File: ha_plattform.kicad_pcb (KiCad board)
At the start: 2 copper layers, 55 x 55 mm, 15 parts, among them J3 Raspberry_Pi_2_3

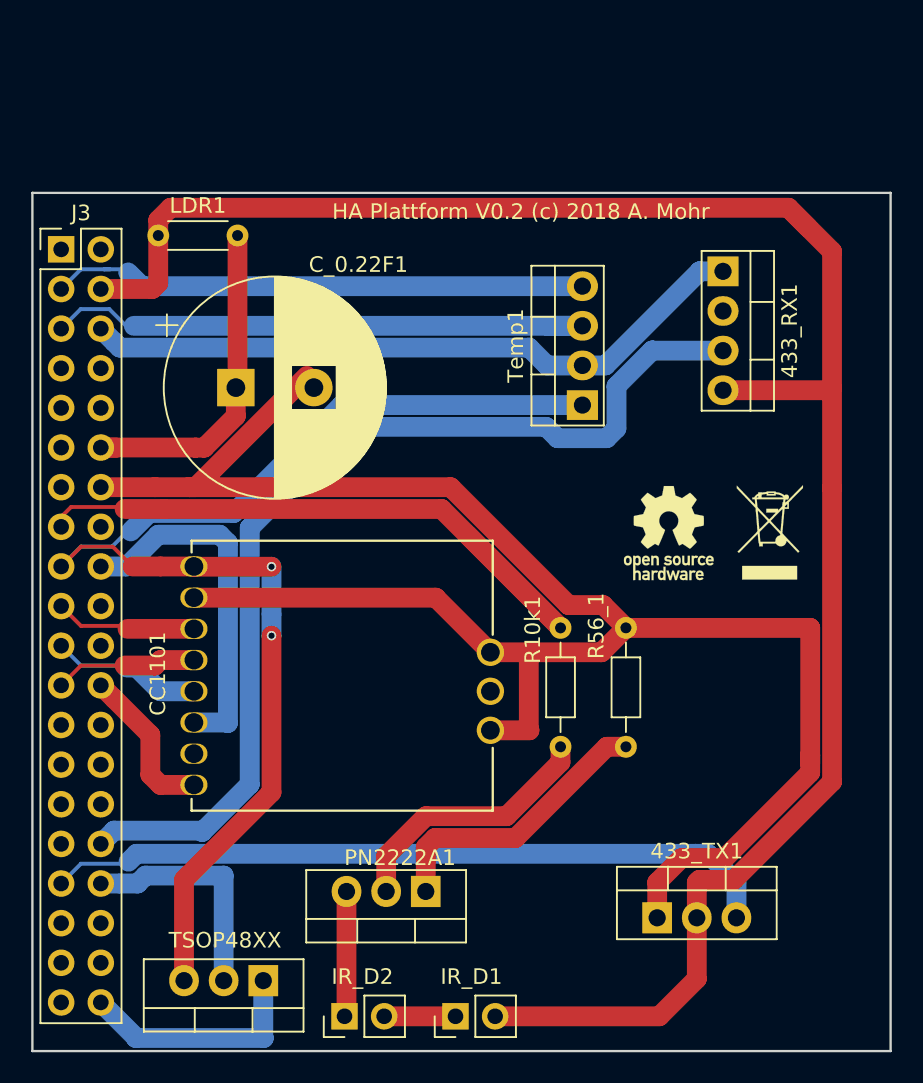
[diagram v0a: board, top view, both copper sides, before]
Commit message: reduced footprint for capacitor
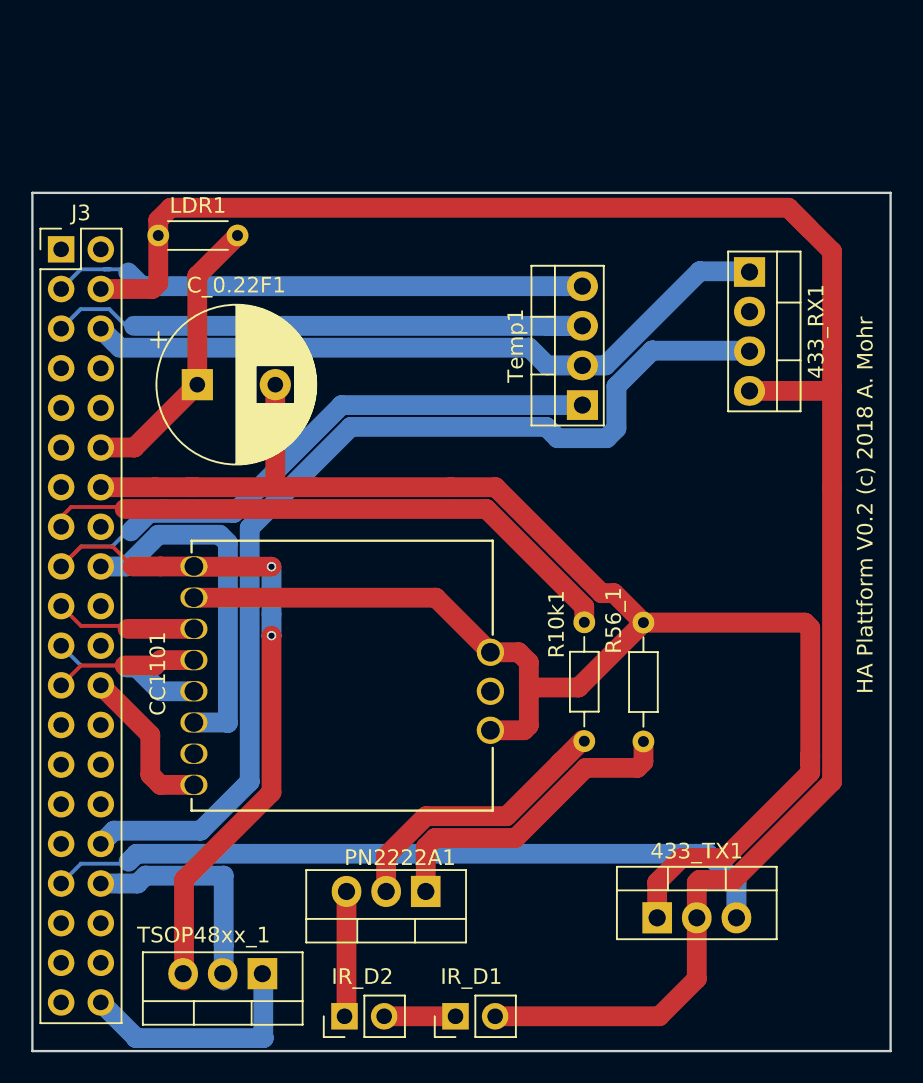
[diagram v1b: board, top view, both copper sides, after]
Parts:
- removed REF**: OSHW-Logo_5.7x6mm_SilkScreen, Symbol:OSHW-Logo_5.7x6mm_SilkScreen
- removed REF**: WEEE-Logo_4.2x6mm_SilkScreen, Symbol:WEEE-Logo_4.2x6mm_SilkScreen
- removed TSOP48XX: TSOP45xx_0, Package_TO_SOT_THT:TO-220-3_Vertical
- added TSOP48xx_1: TSOP45xx_0, Package_TO_SOT_THT:TO-220-3_Vertical, F.Cu at (34.7, 70.0)
- C_0.22F1: footprint Capacitor_THT:CP_Radial_D14.0mm_P5.00mm -> Capacitor_THT:CP_Radial_D10.0mm_P5.00mm
- moved C_0.22F1 2.48 mm to (30.6, 32.3)
- moved 433_RX1 1.70 mm to (66.0, 25.1)
- moved R10k1 1.56 mm to (55.4, 47.5)
- moved R56_1 1.17 mm to (59.2, 55.2)
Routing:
- net Net-(J3-Pad15): track 44.6 -> 38.1 mm
- net Net-(C_0.22F1-Pad1): track 22.1 -> 18.5 mm
- net Net-(PN2222A1-Pad1): track 18.3 -> 20.4 mm
- net Net-(433_TX1-Pad1): track 121.8 -> 120.0 mm
- net Net-(433_RX1-Pad1): track 43.4 -> 45.1 mm
- net Net-(433_RX1-Pad3): track 64.9 -> 66.4 mm
- net Net-(433_RX1-Pad4): track 127.0 -> 125.5 mm
- net Net-(PN2222A1-Pad2): track 16.9 -> 18.0 mm

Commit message: Updated gerber files. Prepared for manufacturing
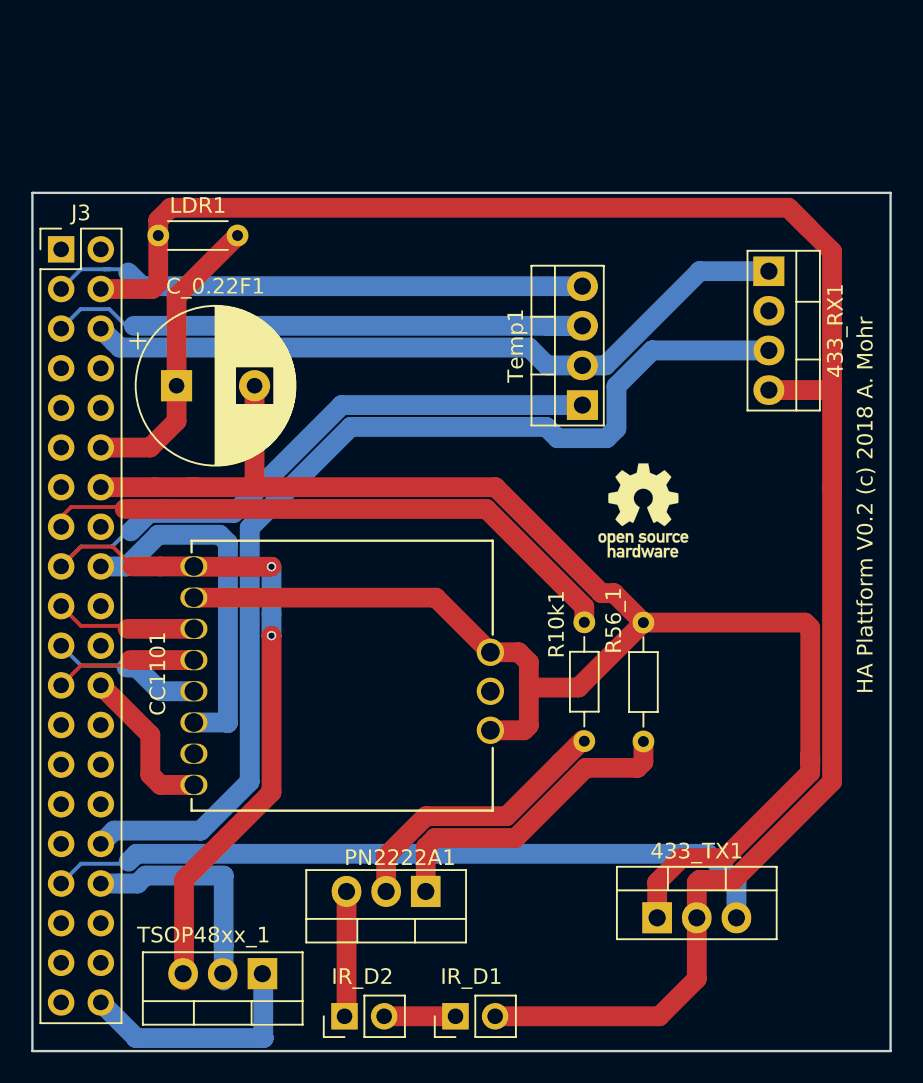
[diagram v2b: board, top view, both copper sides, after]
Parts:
- added REF**: OSHW-Logo_5.7x6mm_SilkScreen, Symbol:OSHW-Logo_5.7x6mm_SilkScreen, F.Cu at (59.1, 40.4)
- moved C_0.22F1 1.33 mm to (29.2, 32.4)
- moved 433_RX1 1.24 mm to (67.2, 25.0)
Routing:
- net Net-(433_RX1-Pad1): track 45.1 -> 46.3 mm
- net Net-(433_RX1-Pad3): track 66.4 -> 67.6 mm
- net Net-(433_RX1-Pad4): track 125.5 -> 124.3 mm
- net Net-(C_0.22F1-Pad1): track 18.5 -> 19.1 mm

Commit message: Fixed layout, so the pinheader are on the correct side...
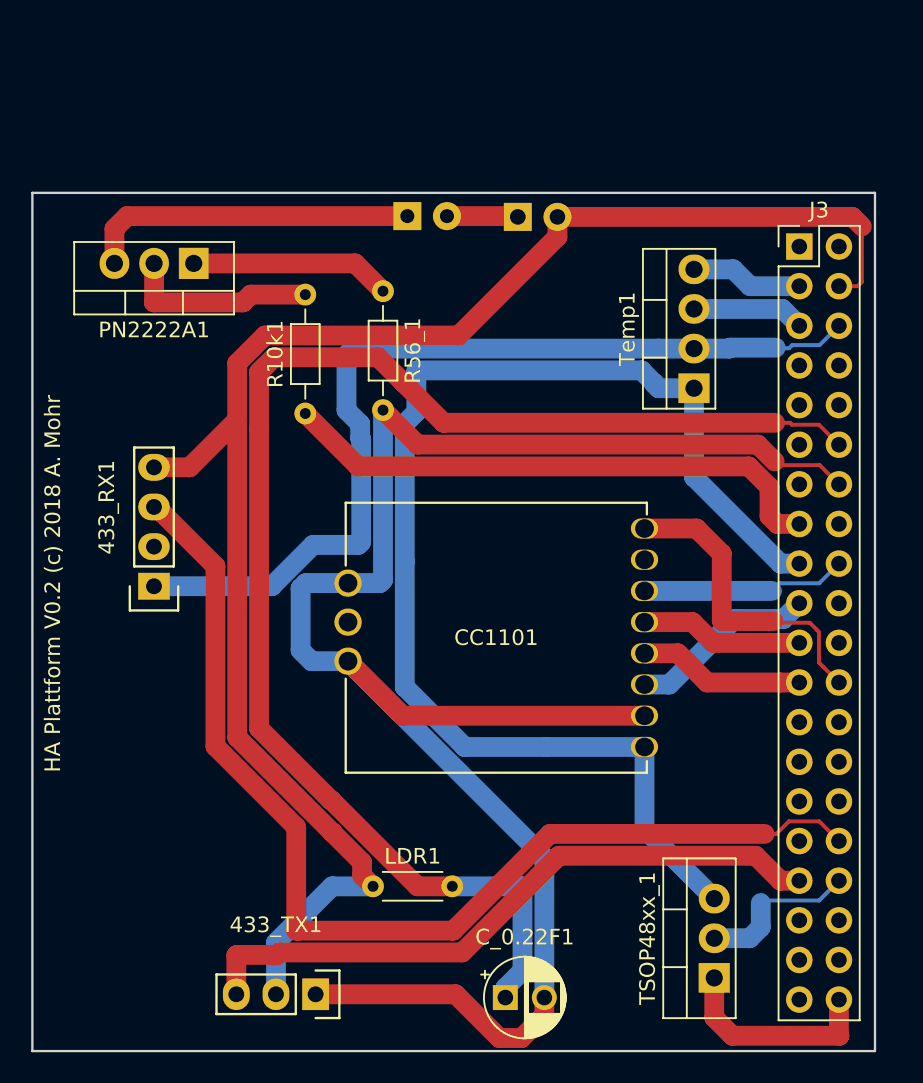
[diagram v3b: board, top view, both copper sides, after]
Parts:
- removed REF**: OSHW-Logo_5.7x6mm_SilkScreen, Symbol:OSHW-Logo_5.7x6mm_SilkScreen
- 433_RX1: footprint Package_TO_SOT_THT:TO-220-4_Vertical -> Sensors:RF_Receiver_433_MHz
- 433_TX1: footprint Package_TO_SOT_THT:TO-220-3_Vertical -> Sensors:RF_Transmitter_433_MHz
- CC1101: footprint cc1101:CC1101-868MHz-Module -> miscellaneous:CC1101-868MHz-Module
- C_0.22F1: footprint Capacitor_THT:CP_Radial_D10.0mm_P5.00mm -> Capacitor_THT:CP_Radial_D5.0mm_P2.50mm
- IR_D1, IR_D2: footprint Connector_PinHeader_2.54mm:PinHeader_1x02_P2.54mm_Vertical -> LED_THT:LED_D3.0mm_Horizontal_O6.35mm_Z10.0mm; moved to B.Cu
- moved IR_D2 51.4 mm to (44.0, 21.5), turned to 0 degrees
- moved IR_D1 51.4 mm to (51.1, 21.5), turned to 0 degrees
- moved J3 47.3 mm to (69.2, 23.4)
- moved C_0.22F1 44.5 mm to (50.3, 71.6)
- moved LDR1 43.9 mm to (41.8, 64.4)
- moved PN2222A1 42.9 mm to (30.3, 24.5)
- moved 433_RX1 42.2 mm to (27.8, 40.1), turned to 90 degrees
- moved R56_1 33.3 mm to (42.5, 26.3), turned to 270 degrees
- moved TSOP48xx_1 29.0 mm to (63.7, 70.3), turned to 90 degrees
- moved 433_TX1 24.9 mm to (35.6, 71.4), turned to 180 degrees
- moved R10k1 22.3 mm to (37.5, 34.1), turned to 90 degrees
- moved CC1101 10.2 mm to (49.7, 48.5), turned to 180 degrees
- moved Temp1 7.23 mm to (62.4, 32.5)
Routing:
- net Net-(C_0.22F1-Pad1): track 19.1 -> 91.9 mm
- net Net-(J3-Pad5): track 36.6 -> 7.20 mm
- net Net-(J3-Pad3): track 34.9 -> 7.20 mm
- net Net-(433_RX1-Pad4): track 124.3 -> 104.8 mm
- net Net-(IR_D2-Pad1): track 8.05 -> 21.3 mm
- net Net-(433_RX1-Pad1): track 46.3 -> 59.2 mm
- net Net-(CC1101-Pad8): track 10.1 -> 20.2 mm
- net Net-(CC1101-Pad6): track 22.9 -> 13.2 mm
- net Net-(PN2222A1-Pad1): track 20.4 -> 12.9 mm
- net Net-(PN2222A1-Pad2): track 18.0 -> 12.4 mm
- net Net-(433_TX1-Pad3): track 47.1 -> 41.9 mm
- net Net-(J3-Pad34): track 14.8 -> 10.4 mm
- net Net-(CC1101-Pad3): track 9.11 -> 12.1 mm
- net Net-(J3-Pad15): track 38.1 -> 35.7 mm
- net Net-(CC1101-Pad4): track 8.69 -> 10.7 mm
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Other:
- board size 55 x 55 mm -> 54 x 55 mm

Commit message: Prepared version 0.3.
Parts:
- added REF**: OSHW-Logo_11.4x12mm_SilkScreen, Symbol:OSHW-Logo_11.4x12mm_SilkScreen, F.Cu at (51.4, 27.7)
- added REF**: WEEE-Logo_4.2x6mm_SilkScreen, Symbol:WEEE-Logo_4.2x6mm_SilkScreen, F.Cu at (22.6, 71.5)
- IR_D1, IR_D2: moved to F.Cu
- moved R56_1 20.6 mm to (23.1, 33.5), turned to 0 degrees
- moved R10k1 8.47 mm to (30.5, 29.4), turned to 180 degrees
- moved IR_D1 5.38 mm to (45.7, 21.4), turned to 180 degrees
- moved 433_RX1 5.31 mm to (27.7, 45.5)
- moved IR_D2 4.02 mm to (40.0, 21.5), turned to 180 degrees
- moved C_0.22F1 2.73 mm to (53.0, 71.5)
- moved Temp1 0.27 mm to (62.4, 32.8)
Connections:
- Temp1 pad 1: Net-(CC1101-Pad1) -> Net-(J3-Pad1)
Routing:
- net Net-(CC1101-Pad1): track 82.2 -> 46.8 mm
- net Net-(433_RX1-Pad1): track 59.2 -> 79.9 mm
- net Net-(433_TX1-Pad1): track 119.7 -> 136.0 mm
- net Net-(J3-Pad1): track 0.00 -> 13.4 mm
- net Net-(IR_D1-Pad1): track 4.56 -> 13.6 mm
- net Net-(J3-Pad15): track 35.7 -> 44.7 mm
- net Net-(433_RX1-Pad4): track 104.8 -> 112.6 mm
- net Net-(PN2222A1-Pad2): track 12.4 -> 8.46 mm
- net Net-(433_RX1-Pad3): track 69.2 -> 66.1 mm
- net Net-(PN2222A1-Pad1): track 12.9 -> 13.8 mm
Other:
- board text added: "HA Plattform V0.3 (c) 2018 A. Mohr"
- board text removed: "HA Plattform V0.2 (c) 2018 A. Mohr"
